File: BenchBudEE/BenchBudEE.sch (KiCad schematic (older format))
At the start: 0 parts

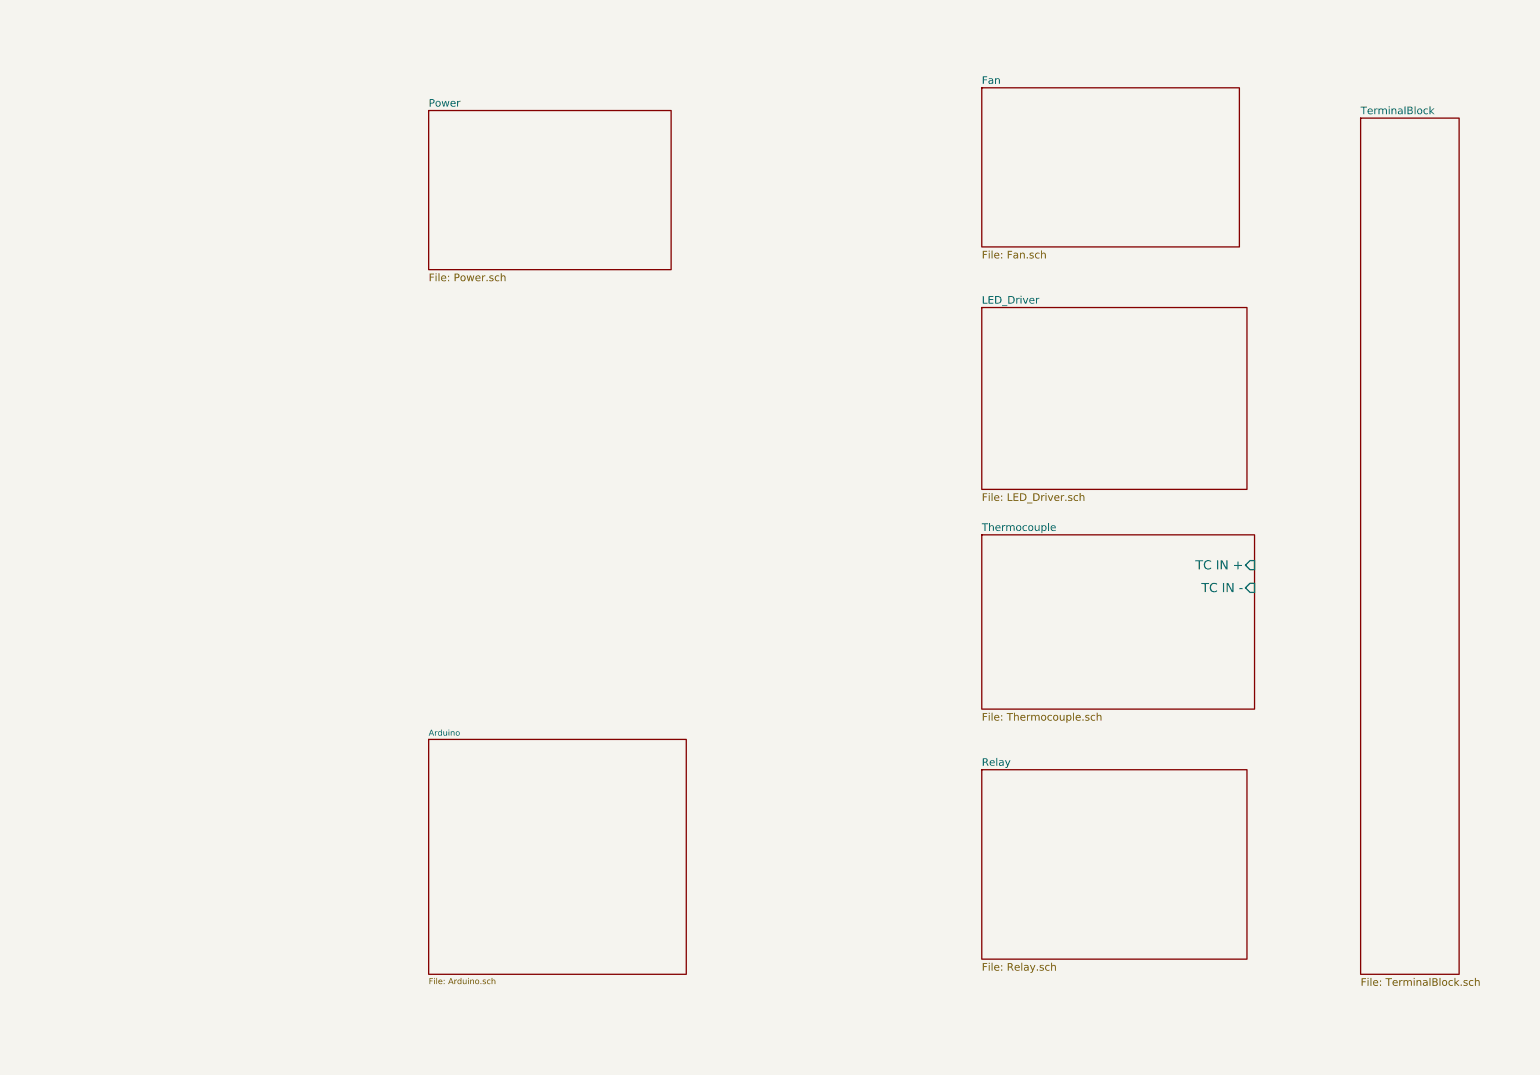
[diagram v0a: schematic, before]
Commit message: Inputs and Outputs added
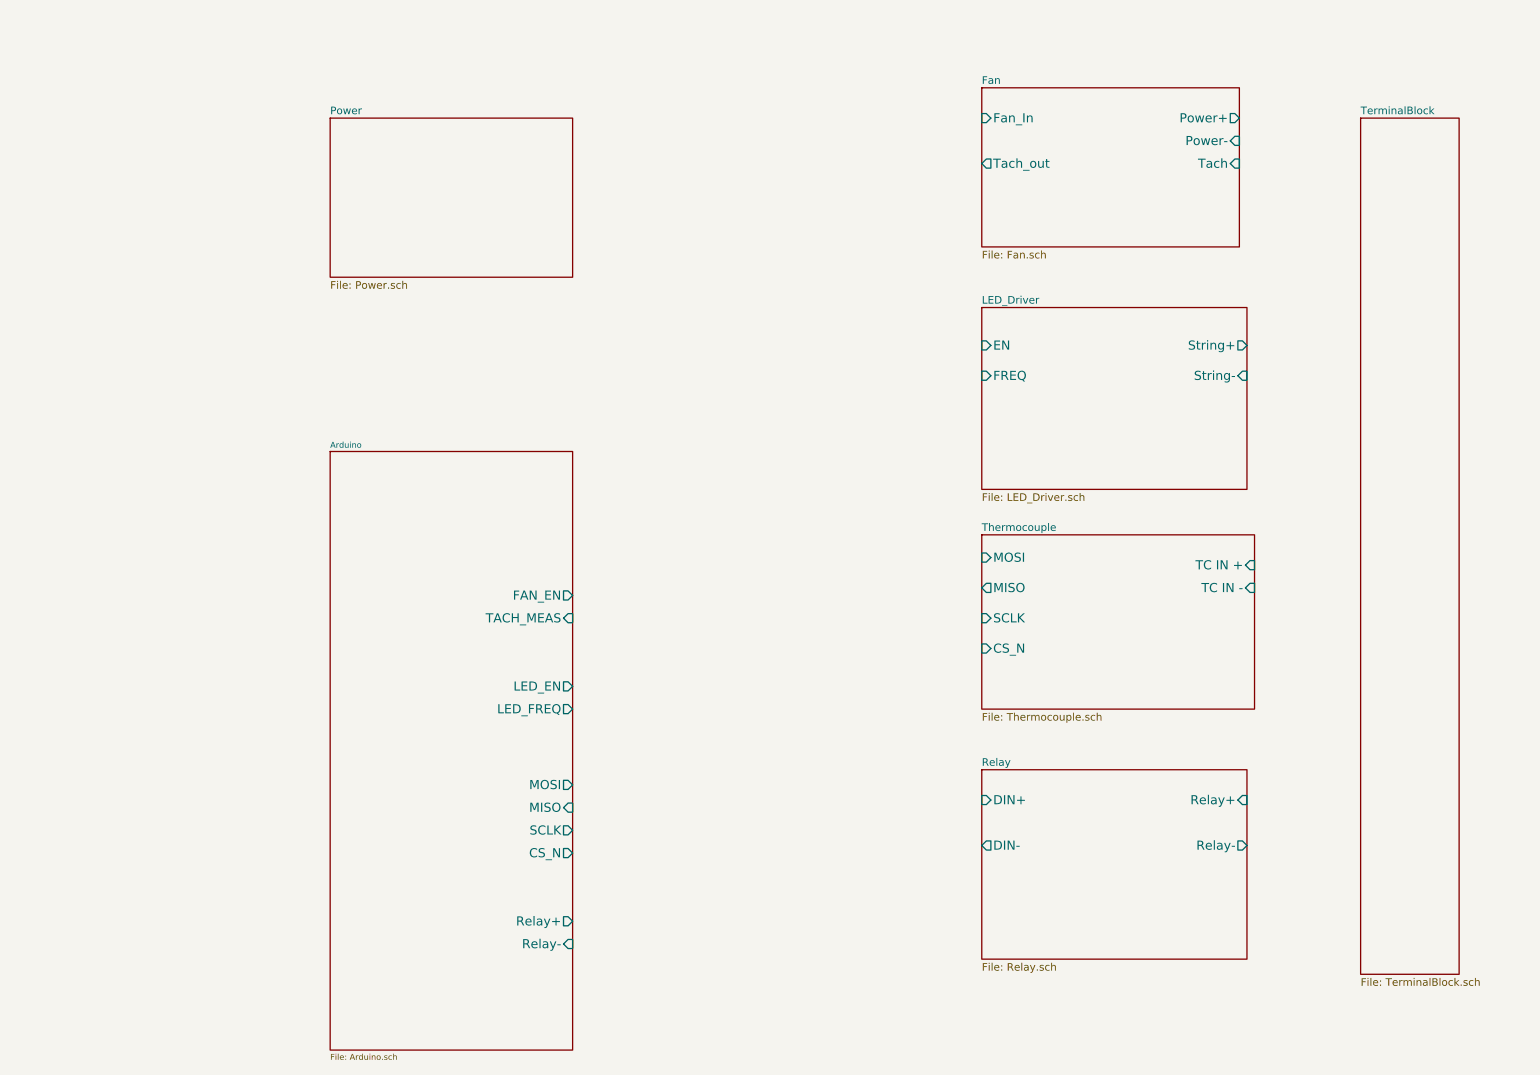
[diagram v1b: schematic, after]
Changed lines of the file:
@@
 $EndDescr
 $Sheet
-S 3450 5400 1700 1550
+S 2800 3500 1600 3950
 U 52ED1BFA
 F0 "Arduino" 39
 F1 "Arduino.sch" 39
+F2 "Relay+" O R 4400 6600 60
+F3 "Relay-" I R 4400 6750 60
+F4 "MOSI" O R 4400 5700 60
+F5 "MISO" I R 4400 5850 60
+F6 "SCLK" O R 4400 6000 60
+F7 "CS_N" O R 4400 6150 60
+F8 "LED_EN" O R 4400 5050 60
+F9 "LED_FREQ" O R 4400 5200 60
+F10 "FAN_EN" O R 4400 4450 60
+F11 "TACH_MEAS" I R 4400 4600 60
 $EndSheet
 $Sheet
@@
 F2 "TC IN +" I R 8900 4250 60
 F3 "TC IN -" I R 8900 4400 60
+F4 "MOSI" I L 7100 4200 60
+F5 "MISO" O L 7100 4400 60
+F6 "SCLK" I L 7100 4600 60
+F7 "CS_N" I L 7100 4800 60
 $EndSheet
 $Sheet
-S 7100 5600 1750 1250
-U 52ED1C4D
-F0 "Relay" 50
-F1 "Relay.sch" 50
-$EndSheet
-$Sheet
-S 3450 1250 1600 1050
+S 2800 1300 1600 1050
 U 52ED1C5C
 F0 "Power" 50
@@
 F0 "LED_Driver" 50
 F1 "LED_Driver.sch" 50
+F2 "EN" I L 7100 2800 60
+F3 "FREQ" I L 7100 3000 60
+F4 "String+" O R 8850 2800 60
+F5 "String-" I R 8850 3000 60
 $EndSheet
 $Sheet
@@
 F0 "Fan" 50
 F1 "Fan.sch" 50
+F2 "Power+" O R 8800 1300 60
+F3 "Power-" I R 8800 1450 60
+F4 "Tach" I R 8800 1600 60
+F5 "Tach_out" O L 7100 1600 60
+F6 "Fan_In" I L 7100 1300 60
 $EndSheet
 $Sheet
@@
 F1 "TerminalBlock.sch" 50
 $EndSheet
+$Sheet
+S 7100 5600 1750 1250
+U 52ED1C4D
+F0 "Relay" 50
+F1 "Relay.sch" 50
+F2 "DIN+" I L 7100 5800 60
+F3 "Relay+" I R 8850 5800 60
+F4 "Relay-" O R 8850 6100 60
+F5 "DIN-" O L 7100 6100 60
+$EndSheet
 $EndSCHEMATC

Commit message: Fan driver block diagram
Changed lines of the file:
@@
 $EndSheet
 $Sheet
-S 7100 1100 1700 1050
+S 7100 1100 1750 1250
 U 52ED1CA7
 F0 "Fan" 50
 F1 "Fan.sch" 50
-F2 "Power+" O R 8800 1300 60
-F3 "Power-" I R 8800 1450 60
-F4 "Tach" I R 8800 1600 60
-F5 "Tach_out" O L 7100 1600 60
-F6 "Fan_In" I L 7100 1300 60
+F2 "Power+" O R 8850 1300 60
+F3 "Power-" I R 8850 1450 60
+F4 "Tach" I R 8850 1600 60
+F5 "Tach_out" O L 7100 2100 60
+F6 "Fan_In" I L 7100 1200 60
+F7 "Current Measure" O L 7100 2000 60
+F8 "MOSI" I L 7100 1400 60
+F9 "MISO" O L 7100 1500 60
+F10 "CS_N" I L 7100 1600 60
+F11 "SCLK" I L 7100 1700 60
 $EndSheet
 $Sheet

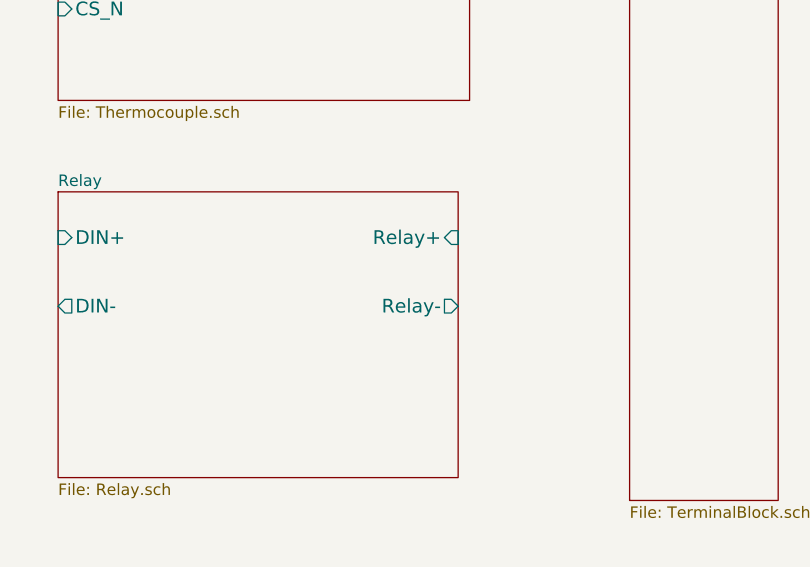
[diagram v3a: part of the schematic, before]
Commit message: Relay block diagram
Relay block diagram and BenchBudEE library created
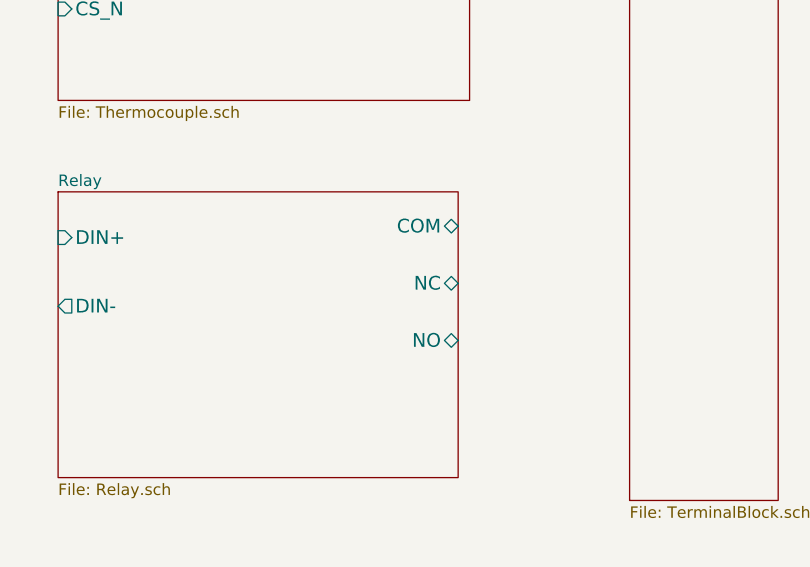
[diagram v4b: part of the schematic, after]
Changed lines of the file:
@@
 LIBS:contrib
 LIBS:valves
+LIBS:BenchBuddy
 LIBS:BenchBudEE-cache
 EELAYER 27 0
@@
 Sheet 1 8
 Title ""
-Date "4 feb 2014"
+Date "8 feb 2014"
 Rev ""
 Comp ""
@@
 F1 "Relay.sch" 50
 F2 "DIN+" I L 7100 5800 60
-F3 "Relay+" I R 8850 5800 60
-F4 "Relay-" O R 8850 6100 60
-F5 "DIN-" O L 7100 6100 60
+F3 "DIN-" O L 7100 6100 60
+F4 "NC" B R 8850 6000 60
+F5 "NO" B R 8850 6250 60
+F6 "COM" B R 8850 5750 60
 $EndSheet
 $EndSCHEMATC

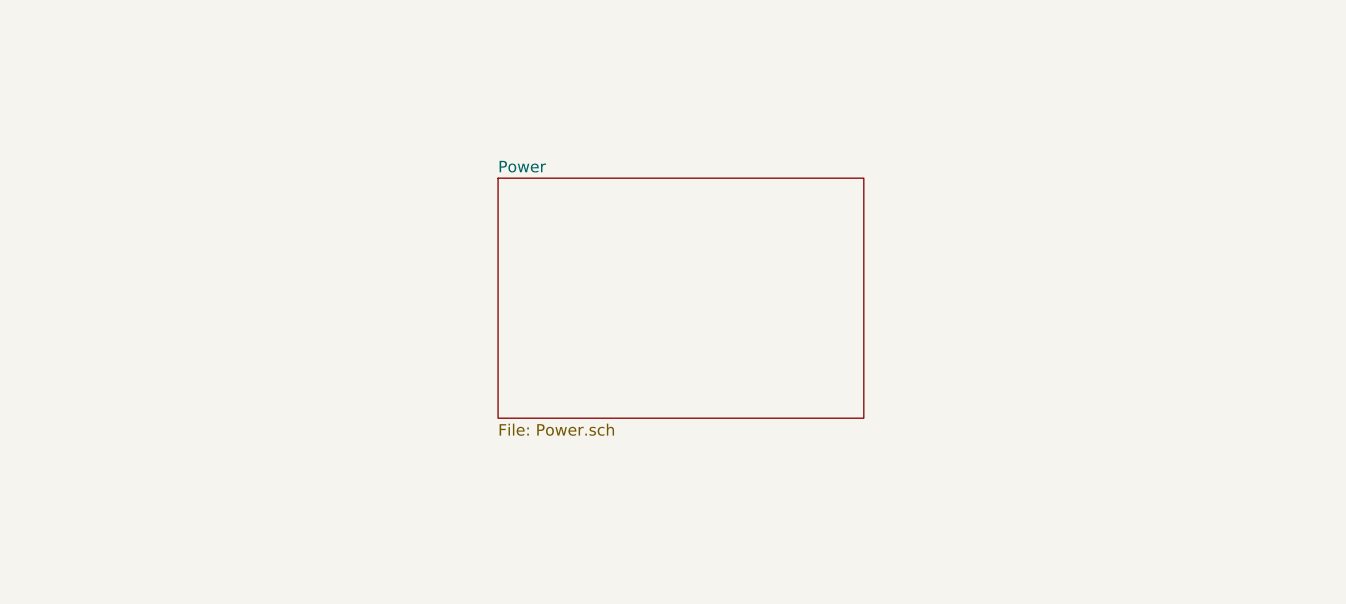
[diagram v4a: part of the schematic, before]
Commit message: Power Protection and filtering module added
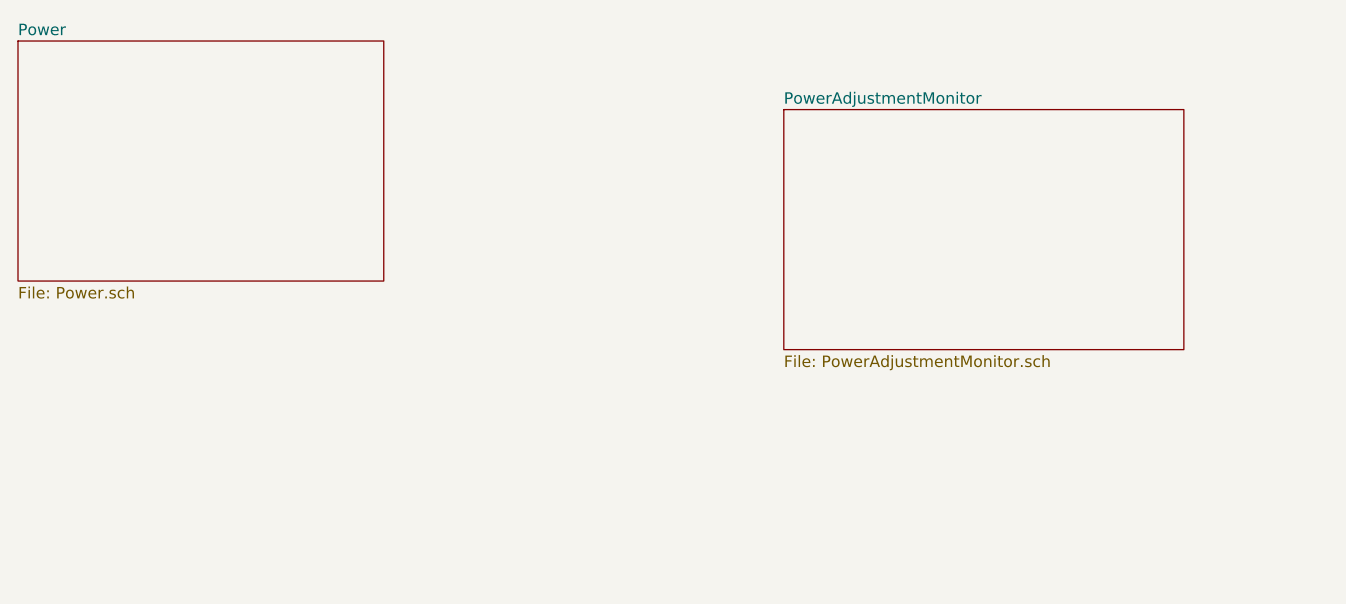
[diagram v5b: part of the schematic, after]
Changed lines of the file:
@@
 $Descr A4 11693 8268
 encoding utf-8
-Sheet 1 8
+Sheet 1 9
 Title ""
 Date "8 feb 2014"
@@
 F6 "SCLK" I L 7100 4600 60
 F7 "CS_N" I L 7100 4800 60
-$EndSheet
-$Sheet
-S 2800 1300 1600 1050
-U 52ED1C5C
-F0 "Power" 50
-F1 "Power.sch" 50
 $EndSheet
 $Sheet
@@
 F6 "COM" B R 8850 5750 60
 $EndSheet
+$Sheet
+S 4050 1000 1750 1050
+U 52F64583
+F0 "PowerAdjustmentMonitor" 50
+F1 "PowerAdjustmentMonitor.sch" 50
+$EndSheet
+$Sheet
+S 700  700  1600 1050
+U 52ED1C5C
+F0 "Power" 50
+F1 "Power.sch" 50
+$EndSheet
 $EndSCHEMATC
